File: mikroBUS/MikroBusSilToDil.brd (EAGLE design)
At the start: 56.8 x 48.2 mm, 2 parts

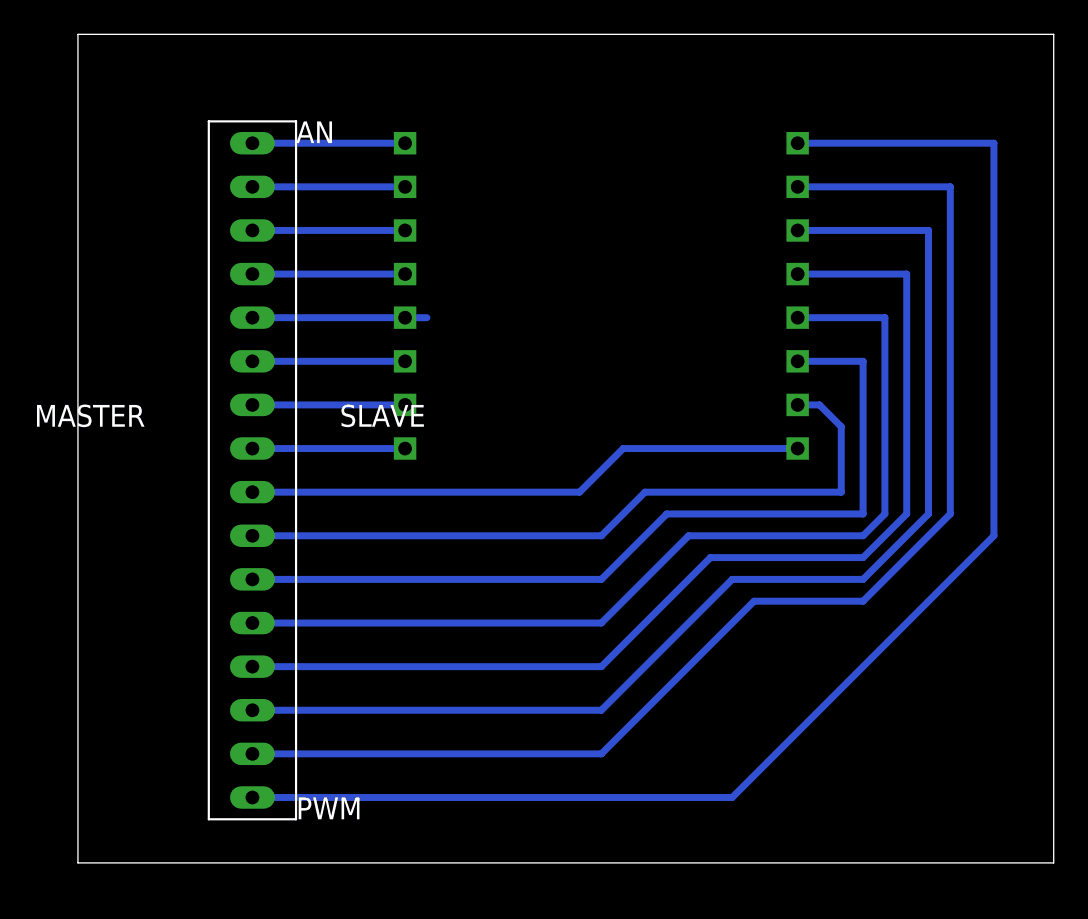
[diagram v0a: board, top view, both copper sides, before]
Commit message: 
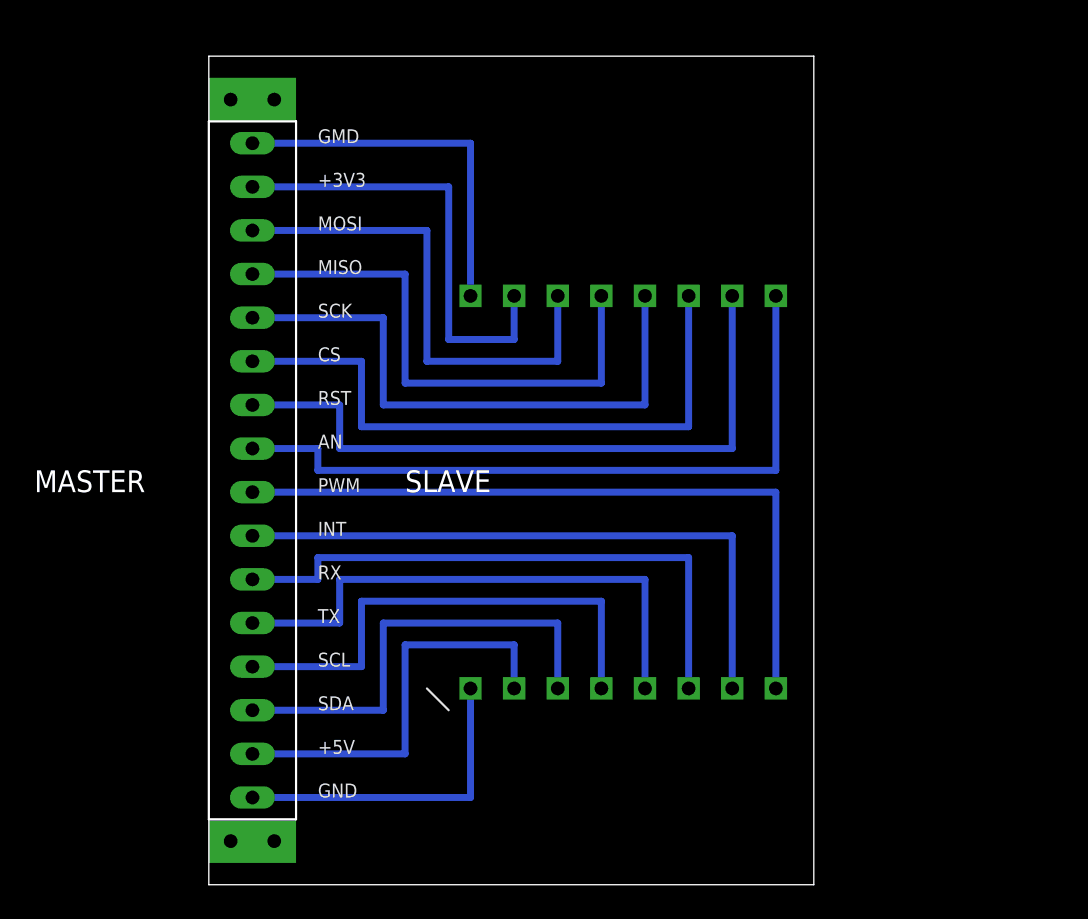
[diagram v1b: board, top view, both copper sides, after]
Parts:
- moved U$1 9.67 mm to (22.9, 64.8), turned to 270 degrees
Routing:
- net N$1: track 83.8 -> 41.9 mm
- net N$2: track 74.4 -> 36.8 mm
- net N$3: track 68.2 -> 34.3 mm
- net N$9: track 8.89 -> 41.9 mm
- net N$10: track 8.89 -> 39.4 mm
- net N$4: track 62.1 -> 31.8 mm
- net N$11: track 8.89 -> 36.8 mm
- net N$5: track 56.0 -> 29.2 mm
- net N$12: track 8.89 -> 34.3 mm
- net N$6: track 49.8 -> 26.7 mm
- net N$13: track 10.2 -> 31.8 mm
- net N$14: track 8.89 -> 29.2 mm
- net N$7: track 42.2 -> 24.1 mm
- net N$15: track 8.89 -> 26.7 mm
- net N$8: track 32.8 -> 19.0 mm
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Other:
- board size 56.8 x 48.2 mm -> 35.2 x 48.2 mm
